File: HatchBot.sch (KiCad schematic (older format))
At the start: 24 parts, among them J1 Trinket_Pro_5V, M1 Motor1, M2 Motor2, P1 DIST SENS, P2 LEFT SENS, P3 RIGHT SENS, P4 LED1, P5 LED2, U1 TB6612FNG

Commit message: Rename “Sumo 1” -> HatchBot.
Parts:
- J1: footprint ArduinoFootprints:Trinket_Pro_5V -> HatchFootprints:Trinket_Pro_5V
- U1: footprint ArduinoFootprints:TB6612FNG -> HatchFootprints:TB6612FNG
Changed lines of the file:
@@
 LIBS:tb6612fng_motor_driver
 LIBS:trinket_pro_5v
-LIBS:MyLib
-LIBS:Sumo 1-cache
+LIBS:HatchLib
+LIBS:HatchBot-cache
 EELAYER 25 0
 EELAYER END
@@
 F 0 "U1" H 4750 5600 60  0000 C CNN
 F 1 "TB6612FNG" H 4750 5500 60  0000 C CNN
-F 2 "ArduinoFootprints:TB6612FNG" H 4750 4700 60  0001 C CNN
+F 2 "HatchFootprints:TB6612FNG" H 4750 4700 60  0001 C CNN
 F 3 "" H 4750 4700 60  0000 C CNN
 	1    4750 4700
@@
 F 0 "J1" H 4700 1800 60  0000 C CNN
 F 1 "Trinket_Pro_5V" H 4750 1700 60  0000 C CNN
-F 2 "ArduinoFootprints:Trinket_Pro_5V" H 4750 1700 60  0001 C CNN
+F 2 "HatchFootprints:Trinket_Pro_5V" H 4750 1700 60  0001 C CNN
 F 3 "" H 4750 1700 60  0000 C CNN
 	1    4750 1700

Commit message: Spin 2, first cut.
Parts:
- removed P4: LED1, Pin_Headers:Pin_Header_Straight_1x03, symbol CONN_01X03
- removed P5: LED2, Pin_Headers:Pin_Header_Straight_1x02, symbol CONN_01X02
- added JP1, JP2: Jumper, Pin_Headers:Pin_Header_Straight_1x02, symbol Jumper
- added LED1, LED2, LED3, LED4: LED, LEDs:LED-3MM, symbol LED
- added R1, R2, R3: 1.2K, Resistors_THT:Resistor_Horizontal_RM7mm, symbol R
- added R4: 270, Resistors_THT:Resistor_Horizontal_RM7mm, symbol R
- C1, C3: footprint Capacitors_ThroughHole:C_Disc_D7.5_P5 -> Capacitors_THT:C_Disc_D7.5_P5
- C2, C4: footprint Capacitors_ThroughHole:C_Radial_D5_L6_P2.5 -> Capacitors_THT:C_Radial_D5_L6_P2.5
- D1, D2, D3, D4, D5, D6, D7, D8: footprint Diodes_ThroughHole:Diode_DO-35_SOD27_Horizontal_RM10 -> Diodes_THT:Diode_DO-35_SOD27_Horizontal_RM10
- LPWR1, M1, M2, MPWR1: footprint Terminal_Blocks:TerminalBlock_Pheonix_PT-3.5mm_2pol -> Connectors_Terminal_Blocks:TerminalBlock_Pheonix_PT-3.5mm_2pol
- P1: footprint Pin_Headers:Pin_Header_Straight_1x03 -> Pin_Headers:Pin_Header_Straight_1x04; symbol SENSOR_CONN -> DIST_SENS_CONN
- P2, P3: symbol SENSOR_CONN -> LIGHT_SENS_CONN
- U1: footprint HatchFootprints:TB6612FNG -> Housings_SSOP:SSOP-24_5.3x8.2mm_Pitch0.65mm
- XP1: footprint Pin_Headers:Pin_Header_Straight_1x08 -> Pin_Headers:Pin_Header_Straight_2x04
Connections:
- net LED1_GREEN is gone; now on net PWMB: J1.11 (~11)
- net LED1_RED is gone; now on net AIN1: J1.3 (~3)
- net +3V3: now also JP2.1; no longer C3.1, C4.1, D1.1 (K), D3.1 (K), D5.1 (K), D7.1 (K), U1.13 (VM2), U1.14 (VM3), U1.24 (VM1)
- net +6V: now also JP1.1; no longer J1.17 (BAT+)
- net A5: now also XP1.3 (P3); no longer XP1.5 (P5)
- net AIN1: no longer J1.13
- net AIN2: now also J1.4; no longer J1.12
- net AREF: now also XP1.7 (P7); no longer XP1.3 (P3)
- net BIN1: now also J1.23 (A3); no longer J1.5 (~5)
- net BIN2: now also J1.24 (A4); no longer J1.4
- net GND: now also P1.4 (GND), XP1.8 (P8), LED1.1 (K), LED2.1 (K), LED3.1 (K), LED4.1 (K); no longer P1.3 (GND), XP1.2 (P2)
- net LED2: now also J1.9 (~9), R2.1; no longer J1.6 (~6)
- net PWMA: now also J1.5 (~5); no longer J1.9 (~9)
- net PWMB: no longer J1.10 (~10)
- net RST: now also XP1.1 (P1); no longer XP1.8 (P8)
- net RX: now also XP1.6 (P6); no longer XP1.7 (P7)
- net STBY: now also J1.12; no longer J1.8
- net TX: now also XP1.4 (P4); no longer XP1.6 (P6)
- net V_LOGIC: now also XP1.2 (P2); no longer XP1.1 (P1)
- net A6: now reaches J1.26 (A6)
- net A6: now also XP1.5 (P5)
- removed net A4: J1.24 (A4), XP1.4 (P4)
- new net: LED1.2 (A), R1.2
- new net: LED2.2 (A), R2.2
- new net: LED3.2 (A), R3.2
- new net: LED4.2 (A), R4.2
- new net LED1: J1.10 (~10), R1.1
- new net LED3: J1.6 (~6), R3.1
- new net TRIG_DIST: J1.8, P1.3 (TRIG)
- new net V_BAT: J1.17 (BAT+), JP1.2
- new net V_MOTOR: C3.1, C4.1, D1.1 (K), D3.1 (K), D5.1 (K), D7.1 (K), JP2.2, R4.1, U1.13 (VM2), U1.14 (VM3), U1.24 (VM1)
- no-connect marks 11 -> 9

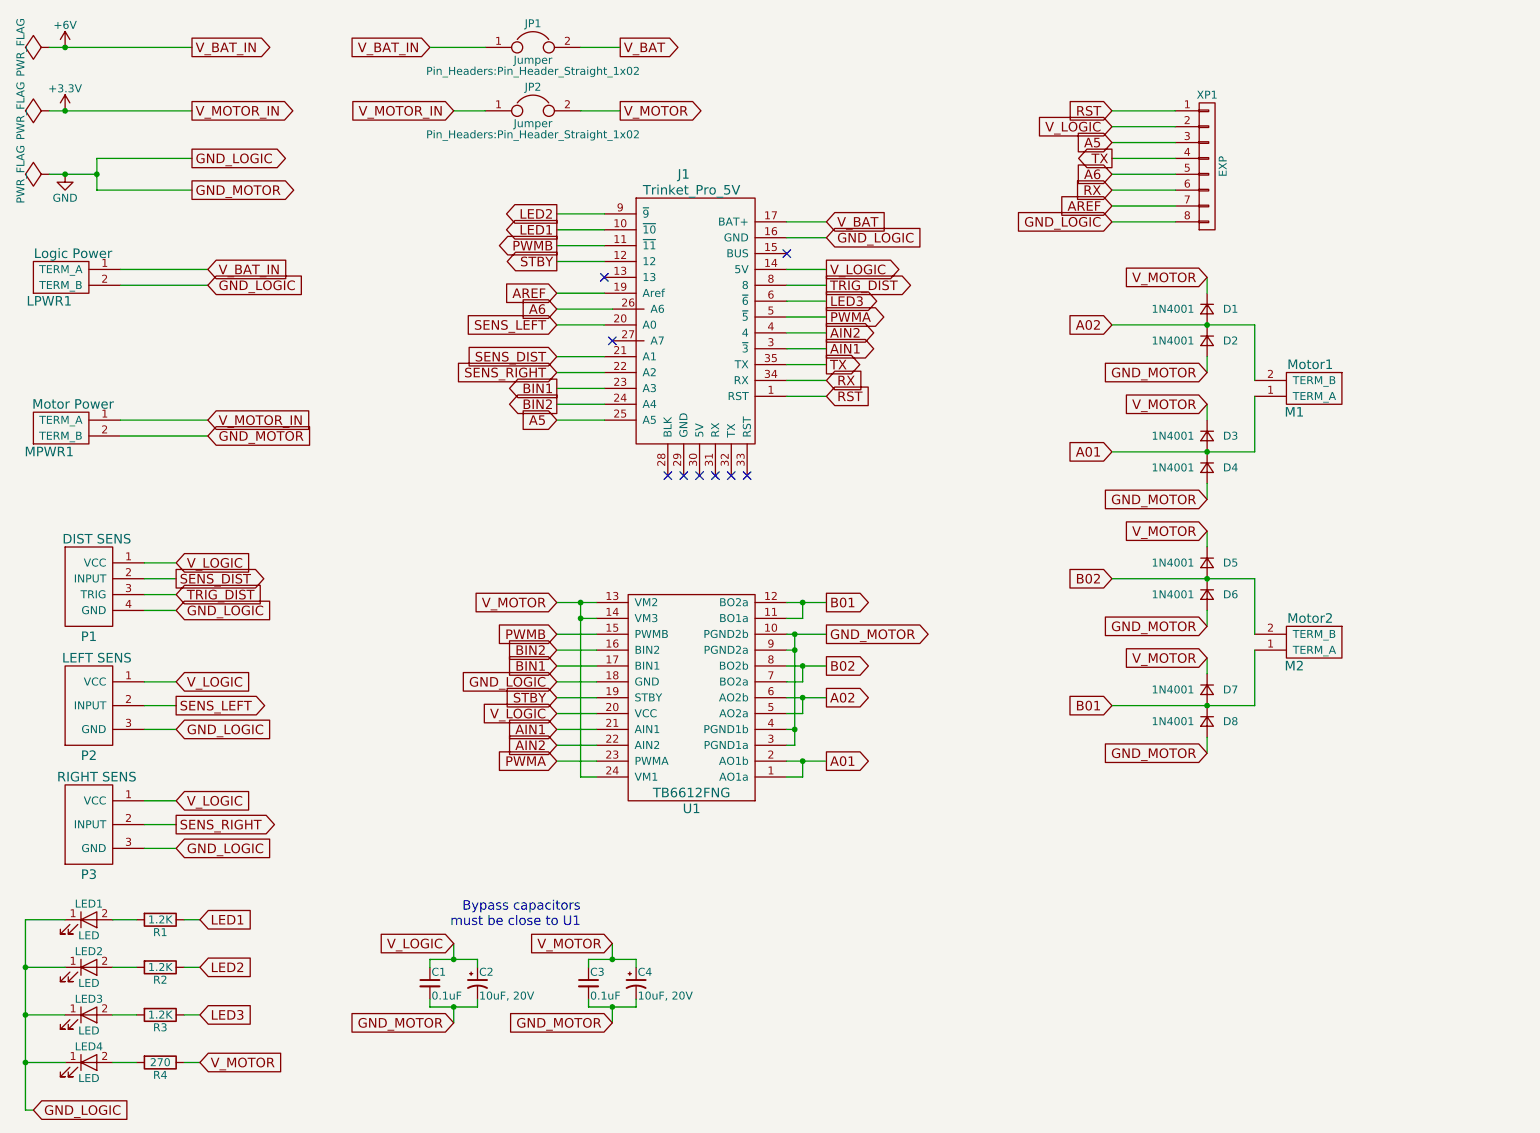
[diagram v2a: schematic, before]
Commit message: Final tweaks (more sane test point placement, switch back to filled zones for doubled pads, add the Hatch logo).
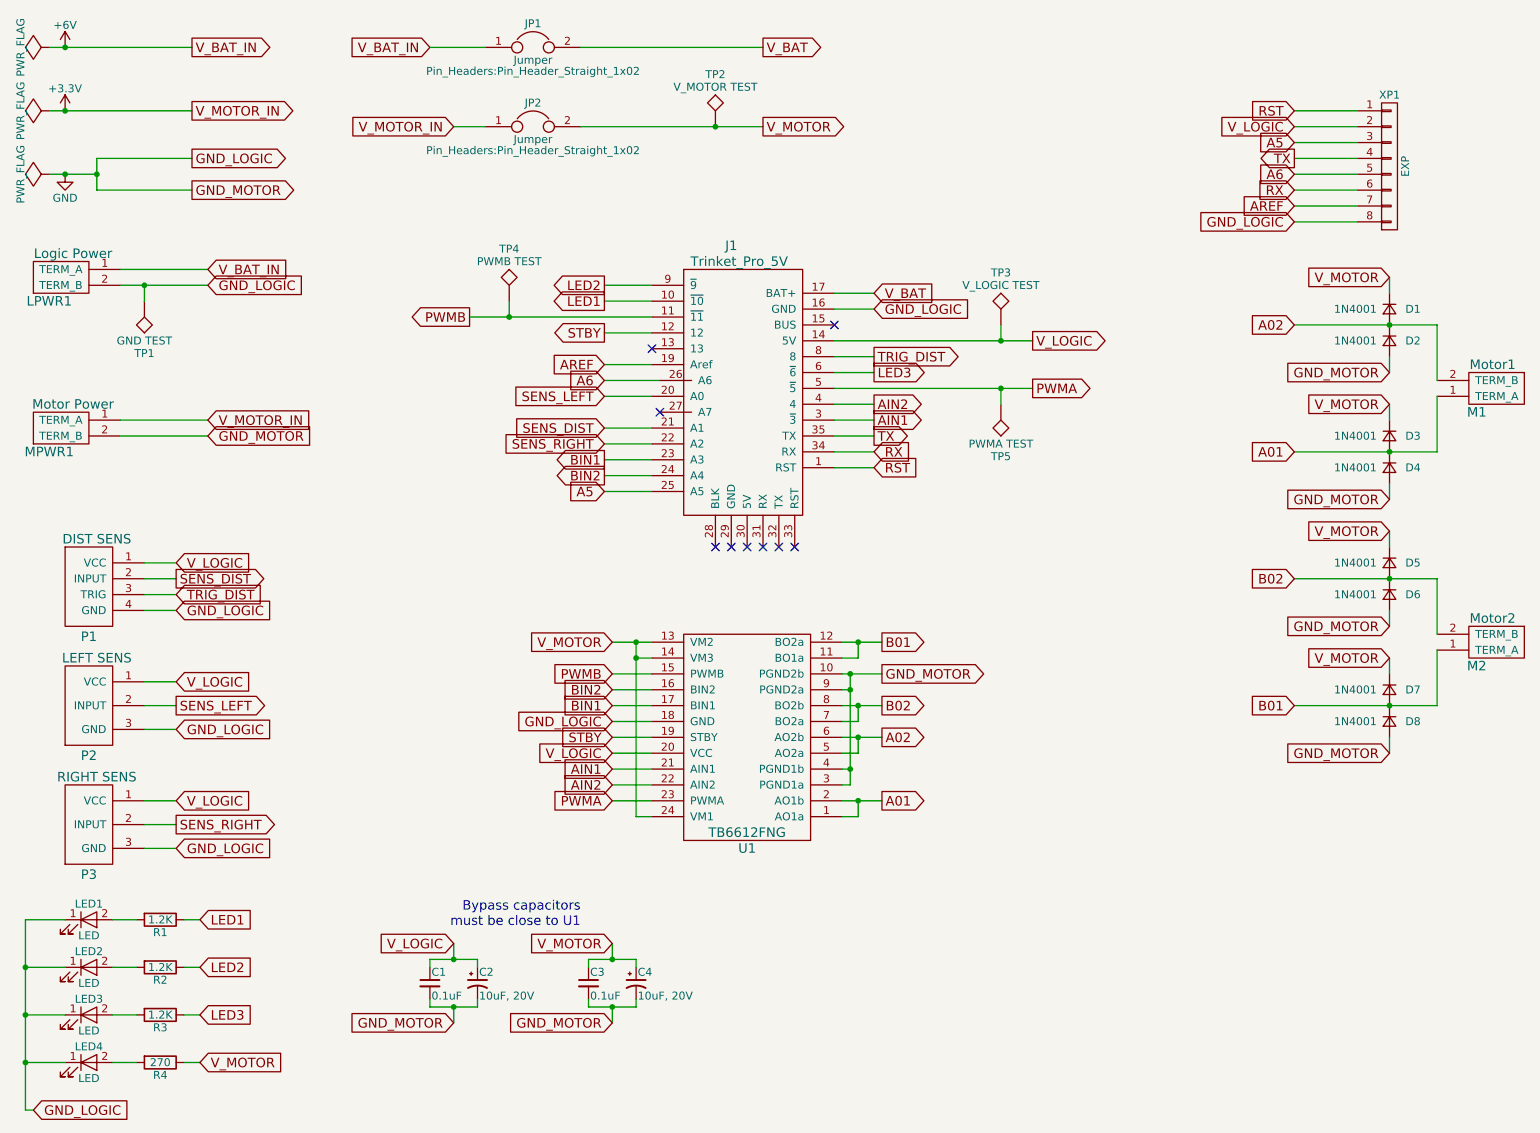
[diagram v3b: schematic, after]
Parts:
- added TP1: GND TEST, Measurement_Points:Measurement_Point_Round-TH_Small, symbol TEST
- added TP2: V_MOTOR TEST, Measurement_Points:Measurement_Point_Round-TH_Small, symbol TEST
- added TP3: V_LOGIC TEST, Measurement_Points:Measurement_Point_Round-TH_Small, symbol TEST
- added TP4: PWMB TEST, Measurement_Points:Measurement_Point_Round-TH_Small, symbol TEST
- added TP5: PWMA TEST, Measurement_Points:Measurement_Point_Round-TH_Small, symbol TEST
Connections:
- net GND: now also TP1.1
- net PWMA: now also TP5.1
- net PWMB: now also TP4.1
- net V_LOGIC: now also TP3.1
- net V_MOTOR: now also TP2.1
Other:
- moved on the sheet: D1, D2, D3, D4, D5, D6, D7, D8, J1, JP2, M1, M2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
